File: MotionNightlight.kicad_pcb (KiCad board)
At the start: 2 copper layers, 72 x 42 mm, 9 parts, among them J1 Conn_02x04_Odd_Even, M2 MountingHole_2.2mm_M2_Pad_Via, Q1 IRL3803

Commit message: v2r1
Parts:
- moved R1 33.8 mm to (125.2, 85.5), turned to 0 degrees
- moved C1 4.62 mm to (109.0, 70.6)
- moved M2 3.06 mm to (162.0, 85.9)
- moved M2 2.66 mm to (98.2, 85.9)
- moved Q1 2.40 mm to (124.2, 75.6)
- moved J1 2.30 mm to (112.8, 79.5)
- moved BT1 2.17 mm to (104.1, 59.6)
- moved M2 1.57 mm to (162.0, 53.2)
- moved M2 0.39 mm to (98.2, 53.2)
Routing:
- net /FET-GATE: track 80.6 -> 34.1 mm
- net /+3.2V: track 14.5 -> 0.00 mm
- net /FET-DRN: track 14.5 -> 0.00 mm, vias 0 -> 38
- added copper zone on F.Cu, net /+3.2V
- added copper zone on B.Cu, net /FET-DRN
- added copper zone on F.Cu, net /FET-DRN
- removed copper zone on B.Cu, net /+3.2V
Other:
- board size 72 x 42 mm -> 70.2 x 39.1 mm
- board text added: "v2r1"
- board text removed: "v1r4"

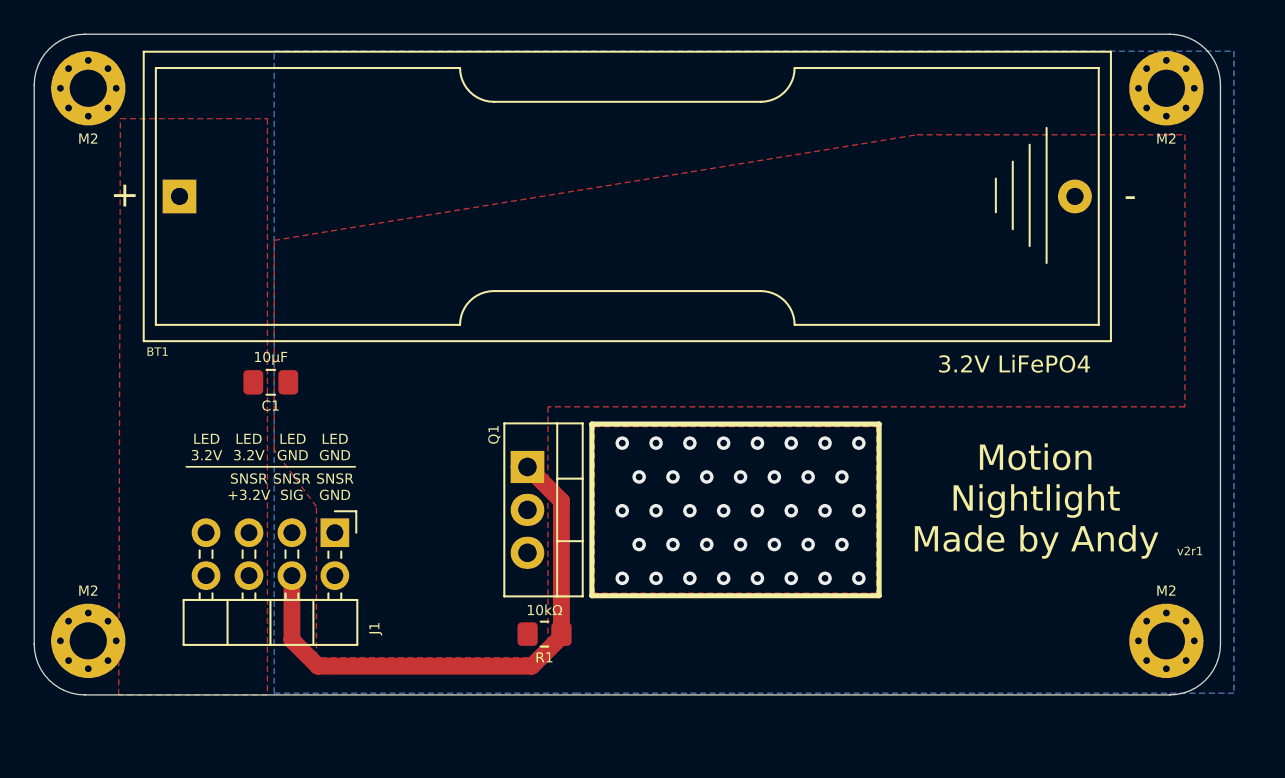
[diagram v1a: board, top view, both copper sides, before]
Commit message: v2r2: Some silkscreen updates, moved the pin header
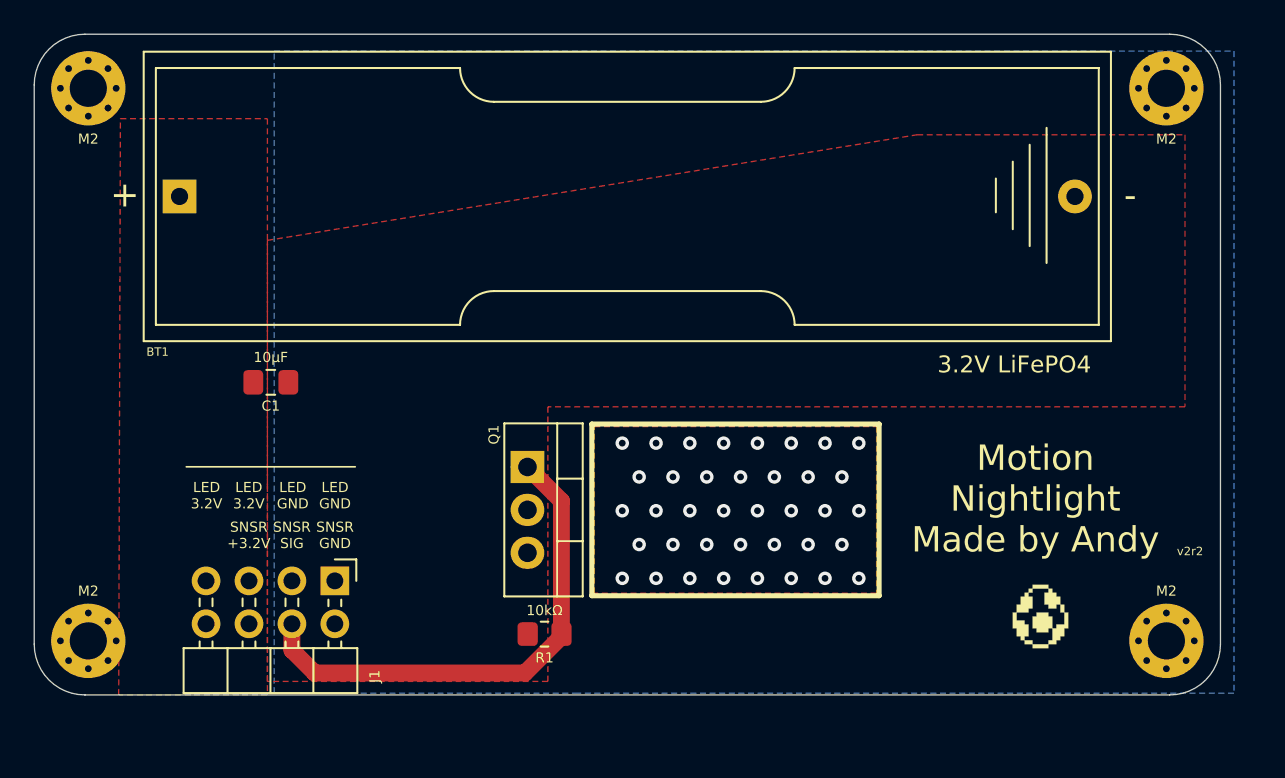
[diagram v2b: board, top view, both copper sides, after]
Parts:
- removed M2 (x4): MountingHole_2.2mm_M2_Pad_Via, MountingHole:MountingHole_2.2mm_M2_Pad_Via
- added G***: LOGO, Andys-Footprints:Yoshi-Egg-Small, F.Cu at (154.6, 84.5)
- added H1: M2, MountingHole:MountingHole_2.2mm_M2_Pad_Via, F.Cu at (98.2, 53.2)
- added H2: M2, MountingHole:MountingHole_2.2mm_M2_Pad_Via, F.Cu at (162.0, 53.2)
- added H3: M2, MountingHole:MountingHole_2.2mm_M2_Pad_Via, F.Cu at (162.0, 85.9)
- added H4: M2, MountingHole:MountingHole_2.2mm_M2_Pad_Via, F.Cu at (98.2, 85.9)
- moved J1 2.85 mm to (112.8, 82.3)
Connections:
- J1 pad 8: (no net) -> unconnected-(J1-Pad8)
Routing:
- net /FET-GATE: track 34.1 -> 32.0 mm
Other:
- net class Default removed
- board text added: "JLCJLCJLCJLC"
- board text added: "v2r2"
- board text removed: "v2r1"
